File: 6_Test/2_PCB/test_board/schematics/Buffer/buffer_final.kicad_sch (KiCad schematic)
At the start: 15 parts, among them U1 SN74ALVCH162827DLR

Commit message: Corrections to schematic 11_20_24
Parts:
- gave numbers to parts that had none: 2
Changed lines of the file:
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@@
 				)
 			)
-			(project "board_main_sim"
-				(path "/9c0580c5-7bd5-4e54-bf4c-826aa4ac3630/49c5ff04-0c5f-41d0-9aa9-a7998c02a6ab"
-					(reference "R10")
+			(project "board_main"
+				(path "/9c0580c5-7bd5-4e54-bf4c-826aa4ac3630/49c5ff04-0c5f-41d0-9aa9-a7998c02a6ab"
+					(reference "R20")
 					(unit 1)
 				)
@@
 				)
 			)
-			(project "board_main_sim"
-				(path "/9c0580c5-7bd5-4e54-bf4c-826aa4ac3630/49c5ff04-0c5f-41d0-9aa9-a7998c02a6ab"
-					(reference "R19")
+			(project "board_main"
+				(path "/9c0580c5-7bd5-4e54-bf4c-826aa4ac3630/49c5ff04-0c5f-41d0-9aa9-a7998c02a6ab"
+					(reference "R29")
 					(unit 1)
 				)
@@
 				)
 			)
-			(project "board_main_sim"
-				(path "/9c0580c5-7bd5-4e54-bf4c-826aa4ac3630/49c5ff04-0c5f-41d0-9aa9-a7998c02a6ab"
-					(reference "R9")
+			(project "board_main"
+				(path "/9c0580c5-7bd5-4e54-bf4c-826aa4ac3630/49c5ff04-0c5f-41d0-9aa9-a7998c02a6ab"
+					(reference "R19")
 					(unit 1)
 				)
@@
 				)
 			)
-			(project "board_main_sim"
-				(path "/9c0580c5-7bd5-4e54-bf4c-826aa4ac3630/49c5ff04-0c5f-41d0-9aa9-a7998c02a6ab"
-					(reference "R12")
+			(project "board_main"
+				(path "/9c0580c5-7bd5-4e54-bf4c-826aa4ac3630/49c5ff04-0c5f-41d0-9aa9-a7998c02a6ab"
+					(reference "R22")
 					(unit 1)
 				)
@@
 				)
 			)
-			(project "board_main_sim"
-				(path "/9c0580c5-7bd5-4e54-bf4c-826aa4ac3630/49c5ff04-0c5f-41d0-9aa9-a7998c02a6ab"
-					(reference "R14")
+			(project "board_main"
+				(path "/9c0580c5-7bd5-4e54-bf4c-826aa4ac3630/49c5ff04-0c5f-41d0-9aa9-a7998c02a6ab"
+					(reference "R24")
 					(unit 1)
 				)
@@
 				)
 			)
-			(project "board_main_sim"
-				(path "/9c0580c5-7bd5-4e54-bf4c-826aa4ac3630/49c5ff04-0c5f-41d0-9aa9-a7998c02a6ab"
-					(reference "R20")
+			(project "board_main"
+				(path "/9c0580c5-7bd5-4e54-bf4c-826aa4ac3630/49c5ff04-0c5f-41d0-9aa9-a7998c02a6ab"
+					(reference "R30")
 					(unit 1)
 				)
@@
 				)
 			)
-			(project "board_main_sim"
-				(path "/9c0580c5-7bd5-4e54-bf4c-826aa4ac3630/49c5ff04-0c5f-41d0-9aa9-a7998c02a6ab"
-					(reference "R13")
+			(project "board_main"
+				(path "/9c0580c5-7bd5-4e54-bf4c-826aa4ac3630/49c5ff04-0c5f-41d0-9aa9-a7998c02a6ab"
+					(reference "R23")
 					(unit 1)
 				)
@@
 		(dnp no)
 		(property "Reference" "R9"
-			(at 84.836 82.042 90)
+			(at 85.09 82.296 90)
 			(effects
 				(font
@@
 				)
 			)
-			(project "board_main_sim"
-				(path "/9c0580c5-7bd5-4e54-bf4c-826aa4ac3630/49c5ff04-0c5f-41d0-9aa9-a7998c02a6ab"
-					(reference "R17")
+			(project "board_main"
+				(path "/9c0580c5-7bd5-4e54-bf4c-826aa4ac3630/49c5ff04-0c5f-41d0-9aa9-a7998c02a6ab"
+					(reference "R27")
 					(unit 1)
 				)
@@
 				)
 			)
-			(project "board_main_sim"
-				(path "/9c0580c5-7bd5-4e54-bf4c-826aa4ac3630/49c5ff04-0c5f-41d0-9aa9-a7998c02a6ab"
-					(reference "R18")
+			(project "board_main"
+				(path "/9c0580c5-7bd5-4e54-bf4c-826aa4ac3630/49c5ff04-0c5f-41d0-9aa9-a7998c02a6ab"
+					(reference "R28")
 					(unit 1)
 				)
@@
 				)
 			)
-			(project "board_main_sim"
-				(path "/9c0580c5-7bd5-4e54-bf4c-826aa4ac3630/49c5ff04-0c5f-41d0-9aa9-a7998c02a6ab"
-					(reference "R15")
+			(project "board_main"
+				(path "/9c0580c5-7bd5-4e54-bf4c-826aa4ac3630/49c5ff04-0c5f-41d0-9aa9-a7998c02a6ab"
+					(reference "R25")
 					(unit 1)
 				)
@@
 				)
 			)
-			(project "board_main_sim"
-				(path "/9c0580c5-7bd5-4e54-bf4c-826aa4ac3630/49c5ff04-0c5f-41d0-9aa9-a7998c02a6ab"
-					(reference "R11")
+			(project "board_main"
+				(path "/9c0580c5-7bd5-4e54-bf4c-826aa4ac3630/49c5ff04-0c5f-41d0-9aa9-a7998c02a6ab"
+					(reference "R21")
 					(unit 1)
 				)
@@
 				)
 			)
-			(project "board_main_sim"
-				(path "/9c0580c5-7bd5-4e54-bf4c-826aa4ac3630/49c5ff04-0c5f-41d0-9aa9-a7998c02a6ab"
-					(reference "U7")
+			(project "board_main"
+				(path "/9c0580c5-7bd5-4e54-bf4c-826aa4ac3630/49c5ff04-0c5f-41d0-9aa9-a7998c02a6ab"
+					(reference "U5")
 					(unit 1)
 				)
@@
 		(on_board yes)
 		(dnp no)
-		(property "Reference" "R?"
+		(property "Reference" "R32"
 			(at 84.836 108.712 90)
 			(effects
@@
 			(project "board_main"
 				(path "/9c0580c5-7bd5-4e54-bf4c-826aa4ac3630/49c5ff04-0c5f-41d0-9aa9-a7998c02a6ab"
-					(reference "R?")
+					(reference "R32")
 					(unit 1)
 				)
@@
 		(on_board yes)
 		(dnp no)
-		(property "Reference" "R?"
+		(property "Reference" "R31"
 			(at 84.836 104.902 90)
 			(effects
@@
 			(project "board_main"
 				(path "/9c0580c5-7bd5-4e54-bf4c-826aa4ac3630/49c5ff04-0c5f-41d0-9aa9-a7998c02a6ab"
-					(reference "R?")
+					(reference "R31")
 					(unit 1)
 				)
@@
 				)
 			)
-			(project "board_main_sim"
-				(path "/9c0580c5-7bd5-4e54-bf4c-826aa4ac3630/49c5ff04-0c5f-41d0-9aa9-a7998c02a6ab"
-					(reference "R16")
-					(unit 1)
-				)
-			)
-		)
-	)
-	(sheet_instances
-		(path "/"
-			(page "1")
-		)
-	)
+			(project "board_main"
+				(path "/9c0580c5-7bd5-4e54-bf4c-826aa4ac3630/49c5ff04-0c5f-41d0-9aa9-a7998c02a6ab"
+					(reference "R26")
+					(unit 1)
+				)
+			)
+		)
+	)

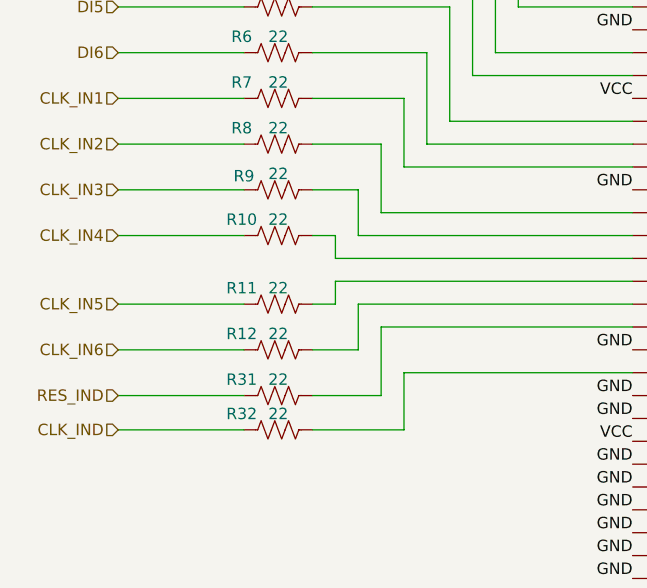
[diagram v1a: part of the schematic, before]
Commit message: Revert "Corrections to schematic 11_20_24"
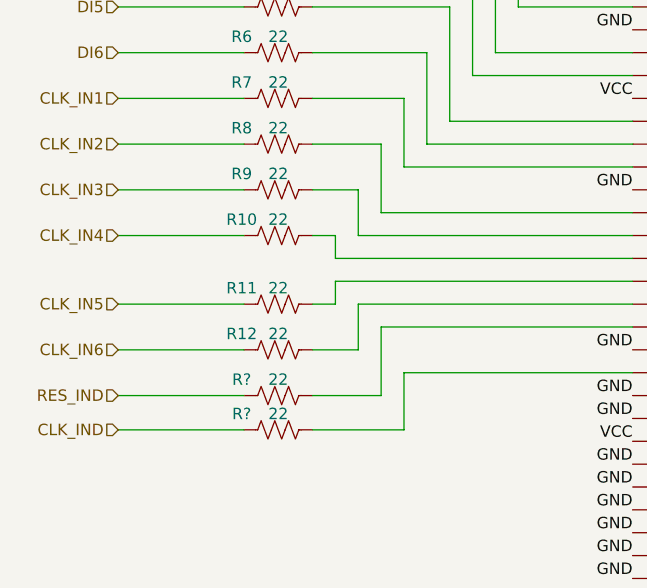
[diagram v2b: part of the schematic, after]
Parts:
- renumbered R32 to R?, R31 to R?
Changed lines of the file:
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@@
 				)
 			)
-			(project "board_main"
-				(path "/9c0580c5-7bd5-4e54-bf4c-826aa4ac3630/49c5ff04-0c5f-41d0-9aa9-a7998c02a6ab"
-					(reference "R20")
+			(project "board_main_sim"
+				(path "/9c0580c5-7bd5-4e54-bf4c-826aa4ac3630/49c5ff04-0c5f-41d0-9aa9-a7998c02a6ab"
+					(reference "R10")
 					(unit 1)
 				)
@@
 				)
 			)
-			(project "board_main"
-				(path "/9c0580c5-7bd5-4e54-bf4c-826aa4ac3630/49c5ff04-0c5f-41d0-9aa9-a7998c02a6ab"
-					(reference "R29")
+			(project "board_main_sim"
+				(path "/9c0580c5-7bd5-4e54-bf4c-826aa4ac3630/49c5ff04-0c5f-41d0-9aa9-a7998c02a6ab"
+					(reference "R19")
 					(unit 1)
 				)
@@
 				)
 			)
-			(project "board_main"
-				(path "/9c0580c5-7bd5-4e54-bf4c-826aa4ac3630/49c5ff04-0c5f-41d0-9aa9-a7998c02a6ab"
-					(reference "R19")
+			(project "board_main_sim"
+				(path "/9c0580c5-7bd5-4e54-bf4c-826aa4ac3630/49c5ff04-0c5f-41d0-9aa9-a7998c02a6ab"
+					(reference "R9")
 					(unit 1)
 				)
@@
 				)
 			)
-			(project "board_main"
-				(path "/9c0580c5-7bd5-4e54-bf4c-826aa4ac3630/49c5ff04-0c5f-41d0-9aa9-a7998c02a6ab"
-					(reference "R22")
+			(project "board_main_sim"
+				(path "/9c0580c5-7bd5-4e54-bf4c-826aa4ac3630/49c5ff04-0c5f-41d0-9aa9-a7998c02a6ab"
+					(reference "R12")
 					(unit 1)
 				)
@@
 				)
 			)
-			(project "board_main"
-				(path "/9c0580c5-7bd5-4e54-bf4c-826aa4ac3630/49c5ff04-0c5f-41d0-9aa9-a7998c02a6ab"
-					(reference "R24")
+			(project "board_main_sim"
+				(path "/9c0580c5-7bd5-4e54-bf4c-826aa4ac3630/49c5ff04-0c5f-41d0-9aa9-a7998c02a6ab"
+					(reference "R14")
 					(unit 1)
 				)
@@
 				)
 			)
-			(project "board_main"
-				(path "/9c0580c5-7bd5-4e54-bf4c-826aa4ac3630/49c5ff04-0c5f-41d0-9aa9-a7998c02a6ab"
-					(reference "R30")
+			(project "board_main_sim"
+				(path "/9c0580c5-7bd5-4e54-bf4c-826aa4ac3630/49c5ff04-0c5f-41d0-9aa9-a7998c02a6ab"
+					(reference "R20")
 					(unit 1)
 				)
@@
 				)
 			)
-			(project "board_main"
-				(path "/9c0580c5-7bd5-4e54-bf4c-826aa4ac3630/49c5ff04-0c5f-41d0-9aa9-a7998c02a6ab"
-					(reference "R23")
+			(project "board_main_sim"
+				(path "/9c0580c5-7bd5-4e54-bf4c-826aa4ac3630/49c5ff04-0c5f-41d0-9aa9-a7998c02a6ab"
+					(reference "R13")
 					(unit 1)
 				)
@@
 		(dnp no)
 		(property "Reference" "R9"
-			(at 85.09 82.296 90)
+			(at 84.836 82.042 90)
 			(effects
 				(font
@@
 				)
 			)
-			(project "board_main"
-				(path "/9c0580c5-7bd5-4e54-bf4c-826aa4ac3630/49c5ff04-0c5f-41d0-9aa9-a7998c02a6ab"
-					(reference "R27")
+			(project "board_main_sim"
+				(path "/9c0580c5-7bd5-4e54-bf4c-826aa4ac3630/49c5ff04-0c5f-41d0-9aa9-a7998c02a6ab"
+					(reference "R17")
 					(unit 1)
 				)
@@
 				)
 			)
-			(project "board_main"
-				(path "/9c0580c5-7bd5-4e54-bf4c-826aa4ac3630/49c5ff04-0c5f-41d0-9aa9-a7998c02a6ab"
-					(reference "R28")
+			(project "board_main_sim"
+				(path "/9c0580c5-7bd5-4e54-bf4c-826aa4ac3630/49c5ff04-0c5f-41d0-9aa9-a7998c02a6ab"
+					(reference "R18")
 					(unit 1)
 				)
@@
 				)
 			)
-			(project "board_main"
-				(path "/9c0580c5-7bd5-4e54-bf4c-826aa4ac3630/49c5ff04-0c5f-41d0-9aa9-a7998c02a6ab"
-					(reference "R25")
+			(project "board_main_sim"
+				(path "/9c0580c5-7bd5-4e54-bf4c-826aa4ac3630/49c5ff04-0c5f-41d0-9aa9-a7998c02a6ab"
+					(reference "R15")
 					(unit 1)
 				)
@@
 				)
 			)
-			(project "board_main"
-				(path "/9c0580c5-7bd5-4e54-bf4c-826aa4ac3630/49c5ff04-0c5f-41d0-9aa9-a7998c02a6ab"
-					(reference "R21")
+			(project "board_main_sim"
+				(path "/9c0580c5-7bd5-4e54-bf4c-826aa4ac3630/49c5ff04-0c5f-41d0-9aa9-a7998c02a6ab"
+					(reference "R11")
 					(unit 1)
 				)
@@
 				)
 			)
-			(project "board_main"
-				(path "/9c0580c5-7bd5-4e54-bf4c-826aa4ac3630/49c5ff04-0c5f-41d0-9aa9-a7998c02a6ab"
-					(reference "U5")
+			(project "board_main_sim"
+				(path "/9c0580c5-7bd5-4e54-bf4c-826aa4ac3630/49c5ff04-0c5f-41d0-9aa9-a7998c02a6ab"
+					(reference "U7")
 					(unit 1)
 				)
@@
 		(on_board yes)
 		(dnp no)
-		(property "Reference" "R32"
+		(property "Reference" "R?"
 			(at 84.836 108.712 90)
 			(effects
@@
 			(project "board_main"
 				(path "/9c0580c5-7bd5-4e54-bf4c-826aa4ac3630/49c5ff04-0c5f-41d0-9aa9-a7998c02a6ab"
-					(reference "R32")
+					(reference "R?")
 					(unit 1)
 				)
@@
 		(on_board yes)
 		(dnp no)
-		(property "Reference" "R31"
+		(property "Reference" "R?"
 			(at 84.836 104.902 90)
 			(effects
@@
 			(project "board_main"
 				(path "/9c0580c5-7bd5-4e54-bf4c-826aa4ac3630/49c5ff04-0c5f-41d0-9aa9-a7998c02a6ab"
-					(reference "R31")
+					(reference "R?")
 					(unit 1)
 				)
@@
 				)
 			)
-			(project "board_main"
-				(path "/9c0580c5-7bd5-4e54-bf4c-826aa4ac3630/49c5ff04-0c5f-41d0-9aa9-a7998c02a6ab"
-					(reference "R26")
-					(unit 1)
-				)
-			)
-		)
-	)
+			(project "board_main_sim"
+				(path "/9c0580c5-7bd5-4e54-bf4c-826aa4ac3630/49c5ff04-0c5f-41d0-9aa9-a7998c02a6ab"
+					(reference "R16")
+					(unit 1)
+				)
+			)
+		)
+	)
+	(sheet_instances
+		(path "/"
+			(page "1")
+		)
+	)
